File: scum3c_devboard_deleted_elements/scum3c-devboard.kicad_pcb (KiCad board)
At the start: 4 copper layers, 30 x 30 mm, 23 parts, among them J1 Conn_01x14, U8 scum3, U9AB1 MPU-9250

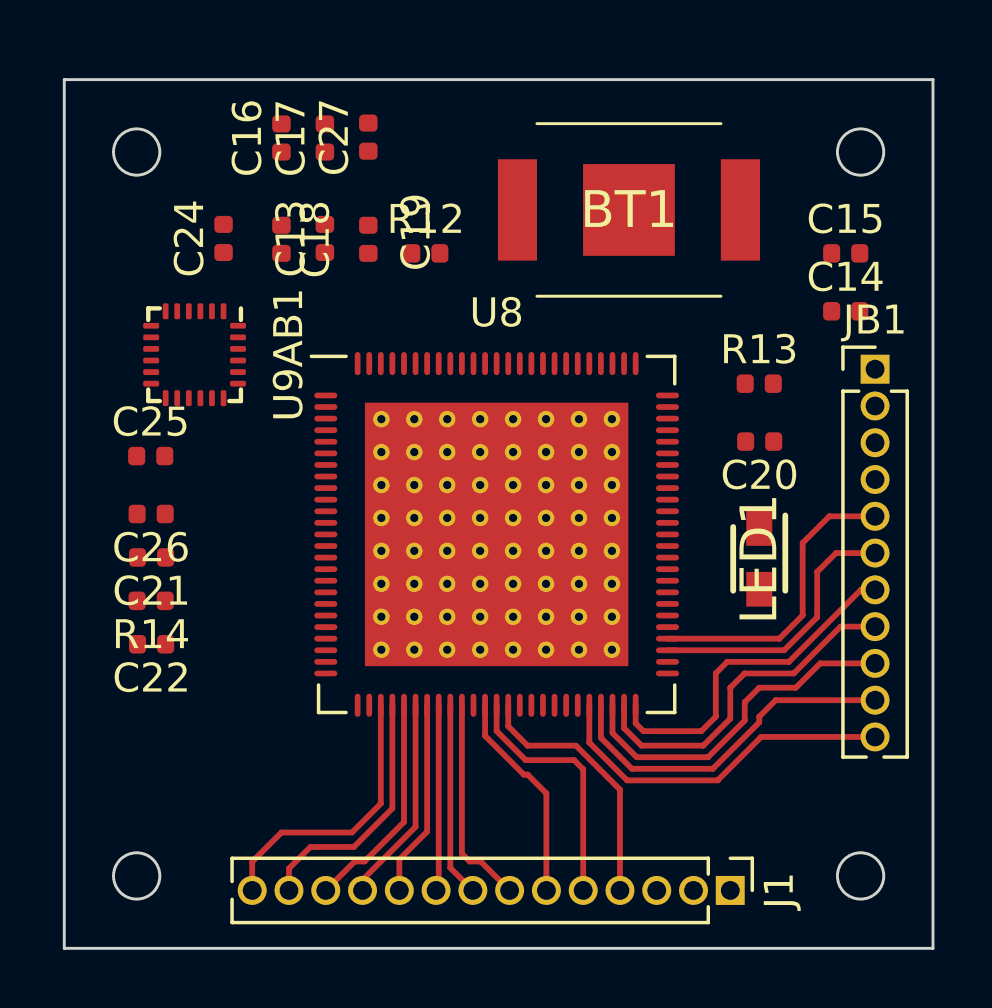
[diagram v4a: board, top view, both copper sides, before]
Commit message: placed vbat
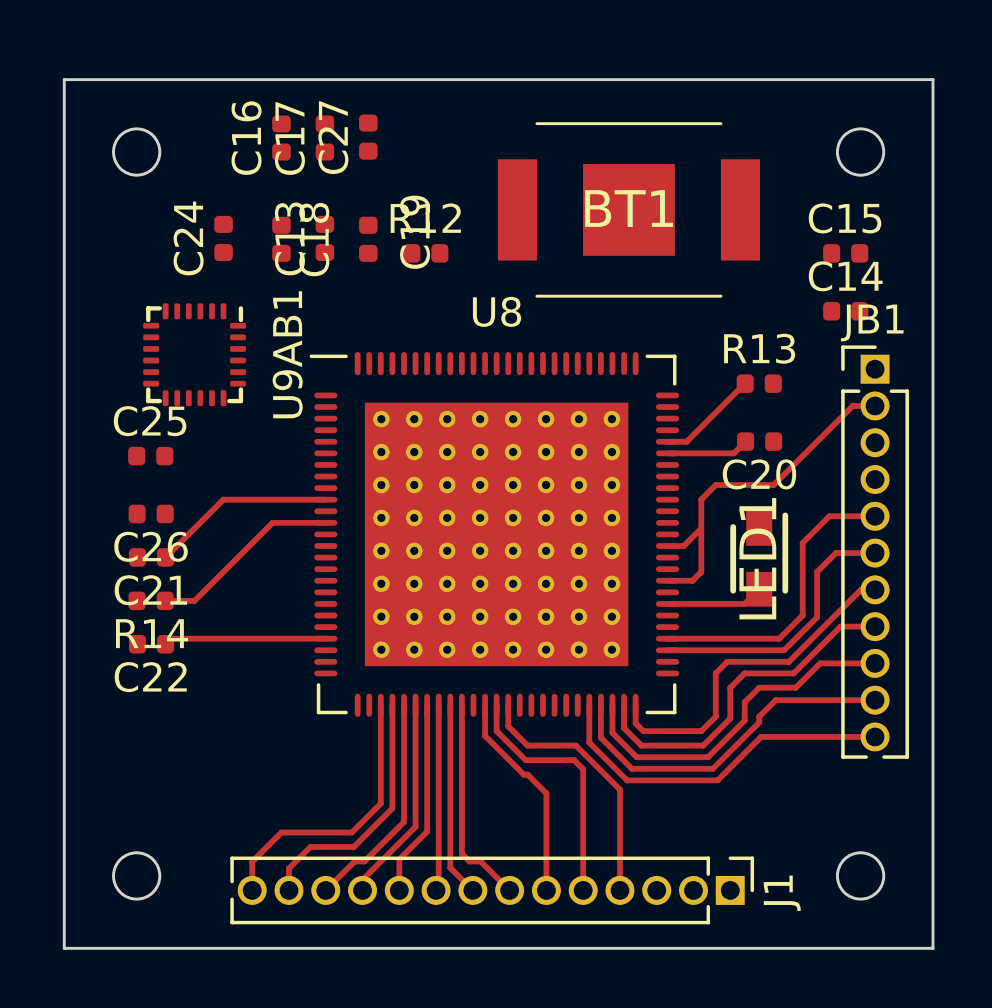
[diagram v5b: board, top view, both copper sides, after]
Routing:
- net +VBAT: track 0.00 -> 12.6 mm
- net Net-(R14-Pad1): track 0.00 -> 6.66 mm
- net +VDD25: track 0.00 -> 6.36 mm
- net Net-(C22-Pad1): track 0.00 -> 5.61 mm
- net Net-(R13-Pad1): track 0.00 -> 3.51 mm
- net Net-(LED1-Pad2): track 0.00 -> 3.38 mm
- net /scumsheet/AUX_LDO_OUTPUT: track 0.00 -> 2.87 mm
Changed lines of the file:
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@@
     (thickness 1.6)
     (drawings 12)
-    (tracks 92)
+    (tracks 115)
     (zones 0)
     (modules 23)
@@
   (gr_line (start 87.5 107.5) (end 87.5 77.5) (layer Edge.Cuts) (width 0.1))
   (gr_line (start 117.5 107.5) (end 87.5 107.5) (layer Edge.Cuts) (width 0.1))
+  (segment (start 114.73 88.77) (end 115.5 88.77) (width 0.2) (layer F.Cu) (net 3))
+  (segment (start 112 91.5) (end 114.73 88.77) (width 0.2) (layer F.Cu) (net 3))
+  (segment (start 109.19375 94.80625) (end 109.5 94.5) (width 0.2) (layer F.Cu) (net 3))
+  (segment (start 108.33125 94.80625) (end 109.19375 94.80625) (width 0.2) (layer F.Cu) (net 3))
+  (segment (start 109.5 94.5) (end 109.5 92) (width 0.2) (layer F.Cu) (net 3))
+  (segment (start 109.5 92) (end 110 91.5) (width 0.2) (layer F.Cu) (net 3))
+  (segment (start 110 91.5) (end 112 91.5) (width 0.2) (layer F.Cu) (net 3))
+  (segment (start 108.33125 93.60625) (end 108.89375 93.60625) (width 0.2) (layer F.Cu) (net 3))
+  (segment (start 108.89375 93.60625) (end 109.5 93) (width 0.2) (layer F.Cu) (net 3))
+  (segment (start 110.62375 90.40625) (end 111.03 90) (width 0.2) (layer F.Cu) (net 6))
+  (segment (start 108.33125 90.40625) (end 110.62375 90.40625) (width 0.2) (layer F.Cu) (net 6))
+  (segment (start 92.99375 92.00625) (end 91 94) (width 0.2) (layer F.Cu) (net 7))
+  (segment (start 96.53125 92.00625) (end 92.99375 92.00625) (width 0.2) (layer F.Cu) (net 7))
+  (segment (start 91.19375 96.80625) (end 91 97) (width 0.2) (layer F.Cu) (net 8))
+  (segment (start 96.53125 96.80625) (end 91.19375 96.80625) (width 0.2) (layer F.Cu) (net 8))
   (segment (start 101.23125 99.10625) (end 101.23125 104.23125) (width 0.2) (layer F.Cu) (net 11))
   (segment (start 101.23125 104.23125) (end 101.5 104.5) (width 0.2) (layer F.Cu) (net 11))
@@
   (segment (start 93.99 104.51) (end 93.99 105.5) (width 0.2) (layer F.Cu) (net 18))
   (segment (start 95 103.5) (end 93.99 104.51) (width 0.2) (layer F.Cu) (net 18))
+  (segment (start 108.33125 90.00625) (end 108.99375 90.00625) (width 0.2) (layer F.Cu) (net 20))
+  (segment (start 111 88) (end 111.015 88) (width 0.2) (layer F.Cu) (net 20))
+  (segment (start 108.99375 90.00625) (end 111 88) (width 0.2) (layer F.Cu) (net 20))
+  (segment (start 90.985 95.5) (end 92 95.5) (width 0.2) (layer F.Cu) (net 21))
+  (segment (start 94.69375 92.80625) (end 92 95.5) (width 0.2) (layer F.Cu) (net 21))
+  (segment (start 96.53125 92.80625) (end 94.69375 92.80625) (width 0.2) (layer F.Cu) (net 21))
   (segment (start 115.011396 95.12) (end 115.5 95.12) (width 0.2) (layer F.Cu) (net 22))
   (segment (start 112.525137 97.60626) (end 115.011396 95.12) (width 0.2) (layer F.Cu) (net 22))
@@
   (segment (start 112.07 98.93) (end 115.5 98.93) (width 0.2) (layer F.Cu) (net 26))
   (segment (start 111.5 99.5) (end 112.07 98.93) (width 0.2) (layer F.Cu) (net 26))
+  (segment (start 110.99375 95.60625) (end 111.5 95.1) (width 0.2) (layer F.Cu) (net 27))
+  (segment (start 108.33125 95.60625) (end 110.99375 95.60625) (width 0.2) (layer F.Cu) (net 27))
   (segment (start 112.359448 97.20625) (end 113.5 96.065698) (width 0.2) (layer F.Cu) (net 28))
   (segment (start 108.33125 97.20625) (end 112.359448 97.20625) (width 0.2) (layer F.Cu) (net 28))

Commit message: delete fill
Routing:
- removed copper zone on In1.Cu, net GND
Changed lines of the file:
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@@
   (segment (start 102.03125 99.10625) (end 102.03125 100.162646) (width 0.2) (layer F.Cu) (net 32))
   (segment (start 102.03125 100.162646) (end 103.368604 101.5) (width 0.2) (layer F.Cu) (net 32))
-  (zone (net 2) (net_name GND) (layer In1.Cu) (hatch edge 0.508)
-    (connect_pads yes (clearance 0.508))
-    (min_thickness 0.254)
-    (fill yes (arc_segments 32) (thermal_gap 0.508) (thermal_bridge_width 0.508))
-    (polygon
-      (pts
-        (xy 117.5 107.5) (xy 87.5 107.5) (xy 87.5 77.5) (xy 117.5 77.5)
-      )
-    )
-  )
 )

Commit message: added layer 1 ground zone
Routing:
- added copper zone on In1.Cu, net GND
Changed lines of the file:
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@@
   (segment (start 102.03125 99.10625) (end 102.03125 100.162646) (width 0.2) (layer F.Cu) (net 32))
   (segment (start 102.03125 100.162646) (end 103.368604 101.5) (width 0.2) (layer F.Cu) (net 32))
+  (zone (net 2) (net_name GND) (layer In1.Cu) (hatch edge 0.508)
+    (connect_pads yes (clearance 0.508))
+    (min_thickness 0.254)
+    (fill yes (arc_segments 32) (thermal_gap 0.508) (thermal_bridge_width 0.508))
+    (polygon
+      (pts
+        (xy 117.5 107.5) (xy 87.5 107.5) (xy 87.5 77.5) (xy 117.5 77.5)
+      )
+    )
+  )
 )

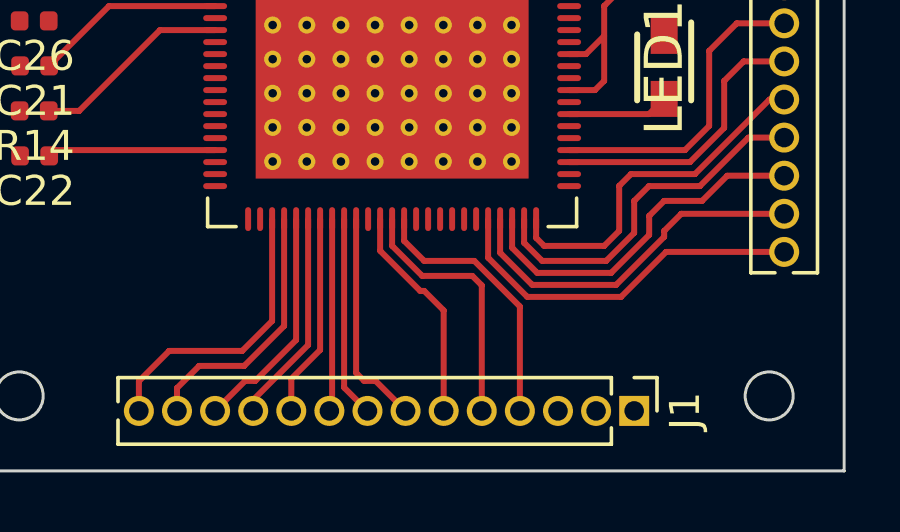
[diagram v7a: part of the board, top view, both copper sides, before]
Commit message: replaced gpio8-10
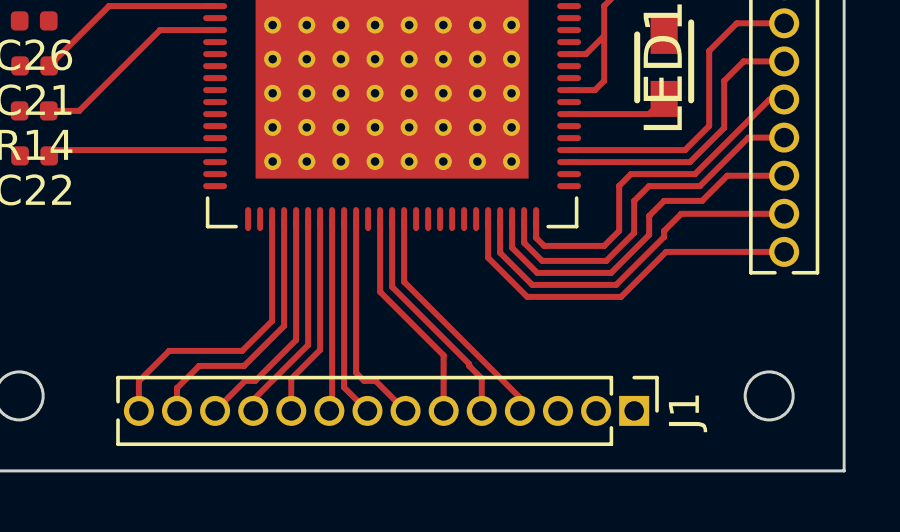
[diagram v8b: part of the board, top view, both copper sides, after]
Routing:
- net /GPIO9: track 8.61 -> 7.63 mm
- net /GPIO10: track 8.97 -> 7.99 mm
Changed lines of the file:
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@@
     (thickness 1.6)
     (drawings 12)
-    (tracks 115)
+    (tracks 111)
     (zones 0)
     (modules 23)
@@
   (segment (start 113.92 92.58) (end 115.5 92.58) (width 0.2) (layer F.Cu) (net 29))
   (segment (start 113 93.5) (end 113.92 92.58) (width 0.2) (layer F.Cu) (net 29))
-  (segment (start 103.5 100.5) (end 105.171508 100.500001) (width 0.2) (layer F.Cu) (net 30))
-  (segment (start 102.83125 99.10625) (end 102.83125 99.83125) (width 0.2) (layer F.Cu) (net 30))
-  (segment (start 106.69 102.018493) (end 106.69 105.5) (width 0.2) (layer F.Cu) (net 30))
-  (segment (start 105.171508 100.500001) (end 106.69 102.018493) (width 0.2) (layer F.Cu) (net 30))
-  (segment (start 102.83125 99.83125) (end 103.5 100.5) (width 0.2) (layer F.Cu) (net 30))
-  (segment (start 105.105809 101) (end 105.42 101.314191) (width 0.2) (layer F.Cu) (net 31))
-  (segment (start 105.42 101.314191) (end 105.42 105.5) (width 0.2) (layer F.Cu) (net 31))
-  (segment (start 103.434302 101) (end 105.105809 101) (width 0.2) (layer F.Cu) (net 31))
-  (segment (start 102.43125 99.10625) (end 102.43125 99.996948) (width 0.2) (layer F.Cu) (net 31))
-  (segment (start 102.43125 99.996948) (end 103.434302 101) (width 0.2) (layer F.Cu) (net 31))
-  (segment (start 104.15 102.15) (end 104.15 105.5) (width 0.2) (layer F.Cu) (net 32))
-  (segment (start 103.5 101.5) (end 104.15 102.15) (width 0.2) (layer F.Cu) (net 32))
-  (segment (start 103.368604 101.5) (end 103.5 101.5) (width 0.2) (layer F.Cu) (net 32))
-  (segment (start 102.03125 99.10625) (end 102.03125 100.162646) (width 0.2) (layer F.Cu) (net 32))
-  (segment (start 102.03125 100.162646) (end 103.368604 101.5) (width 0.2) (layer F.Cu) (net 32))
+  (segment (start 102.83125 101.199854) (end 106.69 105.058604) (width 0.2) (layer F.Cu) (net 30))
+  (segment (start 106.69 105.058604) (end 106.69 105.5) (width 0.2) (layer F.Cu) (net 30))
+  (segment (start 102.83125 99.10625) (end 102.83125 101.199854) (width 0.2) (layer F.Cu) (net 30))
+  (segment (start 102.43125 101.365552) (end 105 103.934302) (width 0.2) (layer F.Cu) (net 31))
+  (segment (start 102.43125 99.10625) (end 102.43125 101.365552) (width 0.2) (layer F.Cu) (net 31))
+  (segment (start 105.42 105.5) (end 105.42 104.42) (width 0.2) (layer F.Cu) (net 31))
+  (segment (start 105 104) (end 105 103.934302) (width 0.2) (layer F.Cu) (net 31))
+  (segment (start 105.42 104.42) (end 105 104) (width 0.2) (layer F.Cu) (net 31))
+  (segment (start 102.03125 99.10625) (end 102.03125 101.53125) (width 0.2) (layer F.Cu) (net 32))
+  (segment (start 104.15 103.65) (end 104.15 105.5) (width 0.2) (layer F.Cu) (net 32))
+  (segment (start 102.03125 101.53125) (end 104.15 103.65) (width 0.2) (layer F.Cu) (net 32))
   (zone (net 2) (net_name GND) (layer In1.Cu) (hatch edge 0.508)
     (connect_pads yes (clearance 0.508))
